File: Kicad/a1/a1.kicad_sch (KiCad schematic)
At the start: 123 parts, among them J1 Conn_02x03_Odd_Even, J2 VGA, J3 AudioJack4, J5 Conn_02x17_Odd_Even, J6 Barrel Jack, J7 DE9_Plug, J8 DE9_Plug, SW1 Q, SW10 P, SW11 A, SW12 S, SW13 D, SW14 F, SW15 G, SW16 H, SW17 J, SW18 K, SW19 L, SW2 W, SW20 ENTER, SW21 Z, SW22 X, SW23 C, SW24 V, SW25 SHIFT, SW26 ALT, SW27 B, SW28 N, SW29 M, SW3 E, SW30 SPACE, SW31 SW_Push, SW32 SW_SPDT, SW4 R, SW5 T, SW6 Y, SW7 U, SW8 I, SW9 O, U1 74HC590A, U10 74HC32, U11 74HC174, U12 74HC4520, U2 74HC590A, U3 62256, U4 SST39SF040, U5 W65C02SxP, U6 74HCT541, U7 74HC166, U8 74HC14, U9 74HC10, Y1 32Mhz

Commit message: Update pcb and readme
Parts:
- removed D37, D38, D5, D6: 1N4148, PCM_Diode_THT_AKL:D_DO-35_SOD27_P7.62mm_Horizontal, symbol PCM_Diode_AKL:1N4148
- removed J5: Conn_02x17_Odd_Even, Connector_IDC:IDC-Header_2x17_P2.54mm_Horizontal, symbol Connector_Generic:Conn_02x17_Odd_Even
- removed RN1: R_Network08, Resistor_THT:R_Array_SIP9, symbol Device:R_Network08
- added J4: Conn_02x17_Odd_Even, Connector_IDC:IDC-Header_2x17_P2.54mm_Horizontal, symbol Connector_Generic:Conn_02x17_Odd_Even
- added RN1: R_Network06, Resistor_THT:R_Array_SIP7, symbol Device:R_Network06
- BZ1: footprint Buzzer_Beeper:MagneticBuzzer_Kingstate_KCG0601 -> Connector_PinHeader_2.54mm:PinHeader_1x02_P2.54mm_Vertical
- D1: footprint LED_THT:LED_D3.0mm -> LED_THT:LED_Rectangular_W5.0mm_H2.0mm
- D10, D11, D12, D13, D14, D15, D16, D17, D18, D19, D20, D21, D22, D23, D24, D25, D26, D27, D28, D29, D30, D31, D32, D33, D34, D35, D36, D7, D8, D9: footprint PCM_Diode_THT_AKL:D_DO-35_SOD27_P7.62mm_Horizontal -> PCM_Diode_THT_AKL_Double:D_DO-35_SOD27_P7.62mm_Horizontal
- D2, D3, D4: footprint PCM_Diode_THT_AKL:D_DO-35_SOD27_P7.62mm_Horizontal -> Diode_THT:D_DO-34_SOD68_P2.54mm_Vertical_KathodeUp
- J3: footprint Connector_Audio:Jack_3.5mm_PJ320E_Horizontal -> Smal:Jack_3.5mm_PJ320A_Horizontal
- R1: value 1MΩ -> 1M; footprint PCM_Resistor_THT_AKL:R_Axial_DIN0204_L3.6mm_D1.6mm_P5.08mm_Horizontal -> PCM_Resistor_THT_AKL_Double:R_Axial_DIN0204_L3.6mm_D1.6mm_P5.08mm_Horizontal
- R11: value 5.6KΩ -> 5.6K; footprint PCM_Resistor_THT_US_AKL:R_Axial_DIN0204_L3.6mm_D1.6mm_P1.90mm_Vertical -> PCM_Resistor_THT_US_AKL:R_Axial_DIN0204_L3.6mm_D1.6mm_P2.54mm_Vertical
- R12, R13: value 27KΩ -> 27K; footprint PCM_Resistor_THT_US_AKL:R_Axial_DIN0204_L3.6mm_D1.6mm_P1.90mm_Vertical -> PCM_Resistor_THT_US_AKL:R_Axial_DIN0204_L3.6mm_D1.6mm_P2.54mm_Vertical
- R14: value 20KΩ -> 20K; footprint PCM_Resistor_THT_US_AKL:R_Axial_DIN0204_L3.6mm_D1.6mm_P1.90mm_Vertical -> PCM_Resistor_THT_US_AKL:R_Axial_DIN0204_L3.6mm_D1.6mm_P2.54mm_Vertical
- R2: value 180Ω -> 180; footprint PCM_Resistor_THT_AKL:R_Axial_DIN0204_L3.6mm_D1.6mm_P5.08mm_Horizontal -> PCM_Resistor_THT_AKL_Double:R_Axial_DIN0204_L3.6mm_D1.6mm_P5.08mm_Horizontal
- R3: value 150Ω -> 150; footprint PCM_Resistor_THT_AKL:R_Axial_DIN0204_L3.6mm_D1.6mm_P5.08mm_Horizontal -> PCM_Resistor_THT_AKL_Double:R_Axial_DIN0204_L3.6mm_D1.6mm_P5.08mm_Horizontal
- R4: value 330Ω -> 330; footprint PCM_Resistor_THT_AKL:R_Axial_DIN0204_L3.6mm_D1.6mm_P5.08mm_Horizontal -> PCM_Resistor_THT_US_AKL:R_Axial_DIN0204_L3.6mm_D1.6mm_P2.54mm_Vertical
- R5: value 100Ω -> 100; footprint PCM_Resistor_THT_US_AKL:R_Axial_DIN0204_L3.6mm_D1.6mm_P1.90mm_Vertical -> PCM_Resistor_THT_US_AKL:R_Axial_DIN0204_L3.6mm_D1.6mm_P2.54mm_Vertical
- SW20: value ENTER -> ENT
- U4: value SST39SF040 -> SST39SF0x0
- Y1: value 32Mhz -> 16Mhz
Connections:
- net COL 3 is gone; now on net A3: SW17.1, SW18.1, SW27.1, SW28.1, SW7.1, SW8.1
- net COL 4 is gone; now on net A4: SW10.1, SW19.1, SW20.1, SW29.1, SW30.1, SW9.1
- net A0: now also SW1.1, SW11.1, SW12.1, SW2.1, SW21.1, SW22.1, J4.11 (Pin_11); no longer D2.1 (K)
- net A1: now also SW13.1, SW14.1, SW23.1, SW24.1, SW3.1, SW4.1, J4.13 (Pin_13); no longer D3.1 (K)
- net A10: now also J4.31 (Pin_31)
- net A11: now also J8.8, J4.33 (Pin_33)
- net A12: now also J7.8, J4.34 (Pin_34)
- net A13: now also D3.2 (A), J4.32 (Pin_32)
- net A14: now also D2.2 (A), J4.30 (Pin_30)
- net A15: now also D4.2 (A), J4.28 (Pin_28)
- net A2: now also SW15.1, SW16.1, SW25.1, SW26.1, SW5.1, SW6.1, J4.15 (Pin_15); no longer D4.1 (K)
- net A3: now also J4.17 (Pin_17)
- net A4: now also J4.19 (Pin_19)
- net A5: now also J4.21 (Pin_21)
- net A6: now also J4.23 (Pin_23)
- net A7: now also J4.25 (Pin_25)
- net A8: now also J4.27 (Pin_27)
- net A9: now also J4.29 (Pin_29)
- net D0: now also J4.12 (Pin_12)
- net D1: now also J4.14 (Pin_14)
- net D2: now also J4.16 (Pin_16)
- net D3: now also J4.18 (Pin_18)
- net D4: now also J4.20 (Pin_20)
- net D5: now also J4.22 (Pin_22)
- net D6: now also J4.24 (Pin_24)
- net D7: now also J4.26 (Pin_26)
- net GND: now also J7.5, J8.5, R13.1, U12.1 (CK), J4.1 (Pin_1); no longer J2.15, R13.2, U11.1 (~{Mr})
- net HROW 0: now also RN1.7 (R6)
- net HROW 1: now also RN1.5 (R4)
- net HROW 2: now also RN1.4 (R3)
- net HROW 3: now also RN1.3 (R2)
- net HROW 4: now also RN1.6 (R5)
- net HROW 5: now also RN1.2 (R1)
- net M16: now also R1.2, R2.2, U12.2 (Enable), U8.8, J4.3 (Pin_3); no longer U12.3 (Q1)
- net M2: now also U12.5 (Q3); no longer U12.6 (Q4)
- net M4: now also U12.4 (Q2); no longer U12.5 (Q3)
- net M8: now also U12.3 (Q1); no longer U12.4 (Q2)
- net RAMHIDE: now also J4.7 (Pin_7)
- net V512: now also D2.1 (K), D3.1 (K), D4.1 (K)
- net VCC: now also J7.7, J8.7, U11.1 (~{Mr}), J4.2 (Pin_2), RN1.1 (common); no longer U12.2 (Enable)
- net r/~{w}: now also J4.10 (Pin_10)
- net ~{A13}: now also J4.9 (Pin_9)
- net ~{A15}: now also J4.8 (Pin_8)
- net ~{NMI}: now also J4.6 (Pin_6)
- net ~{RESET}: now also J4.5 (Pin_5)
- net ø2: now also J4.4 (Pin_4)
- net at R12.1, SW31.1: now also R13.2; no longer R13.1
- removed net COL 0: D2.2 (A), SW1.1, SW11.1, SW12.1, SW2.1, SW21.1, SW22.1
- removed net COL 1: D3.2 (A), SW13.1, SW14.1, SW23.1, SW24.1, SW3.1, SW4.1
- removed net COL 2: D4.2 (A), SW15.1, SW16.1, SW25.1, SW26.1, SW5.1, SW6.1
- no-connect marks 19 -> 17
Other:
- moved on the sheet: J1, R13, RN3

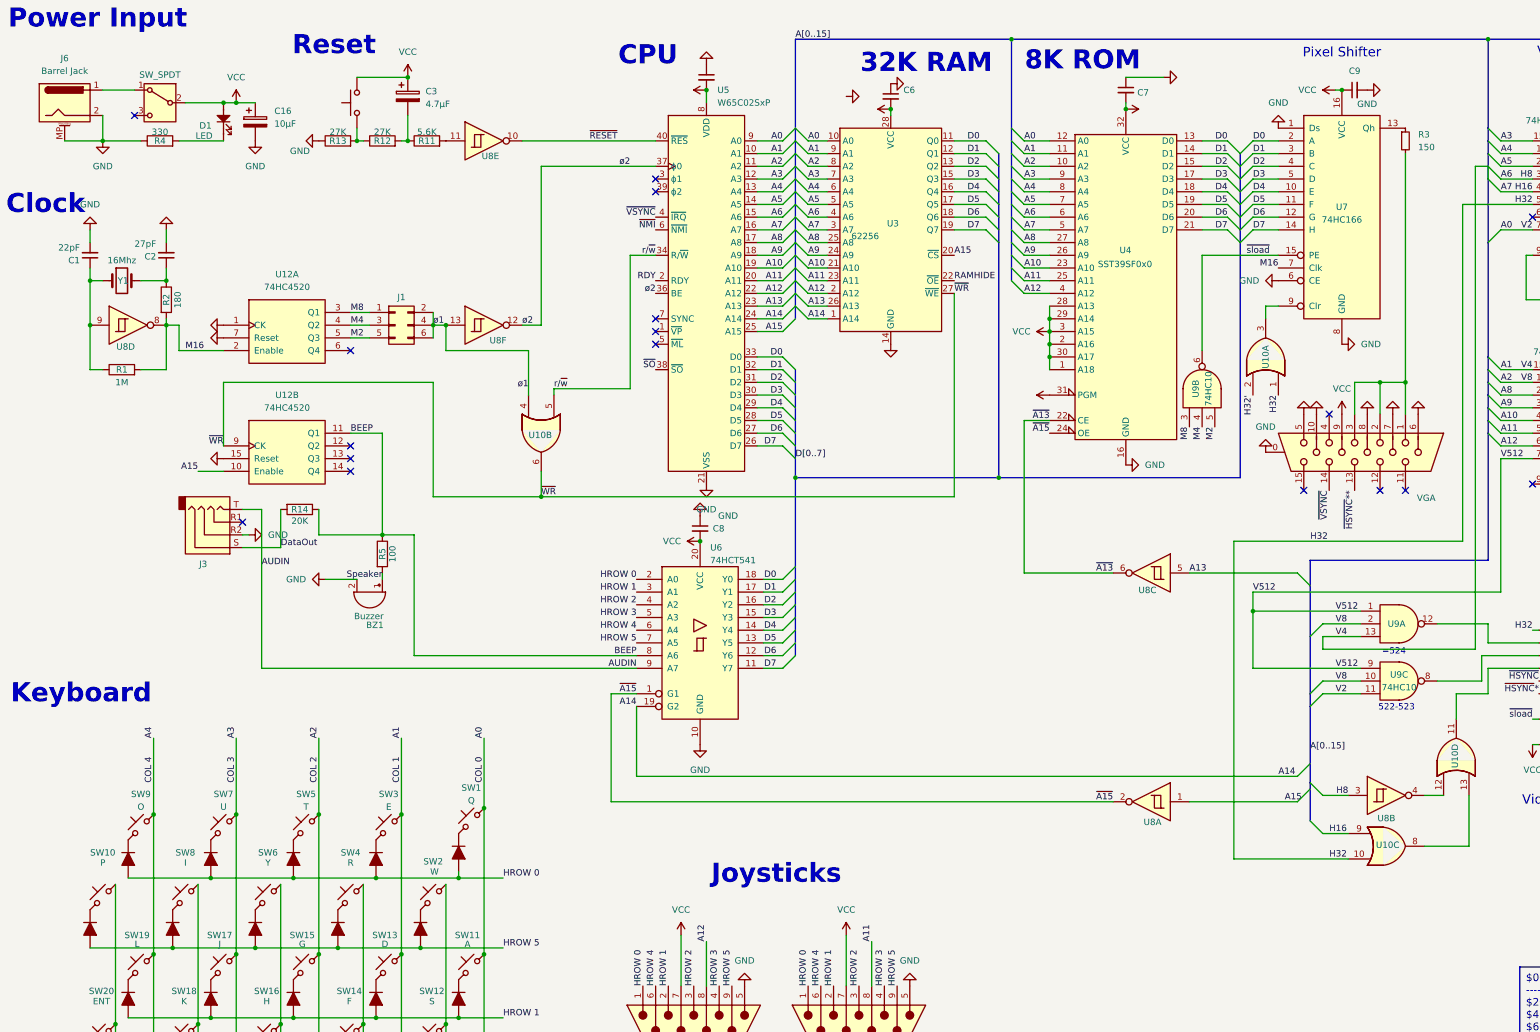
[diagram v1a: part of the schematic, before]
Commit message: tweak pcb, change key layout
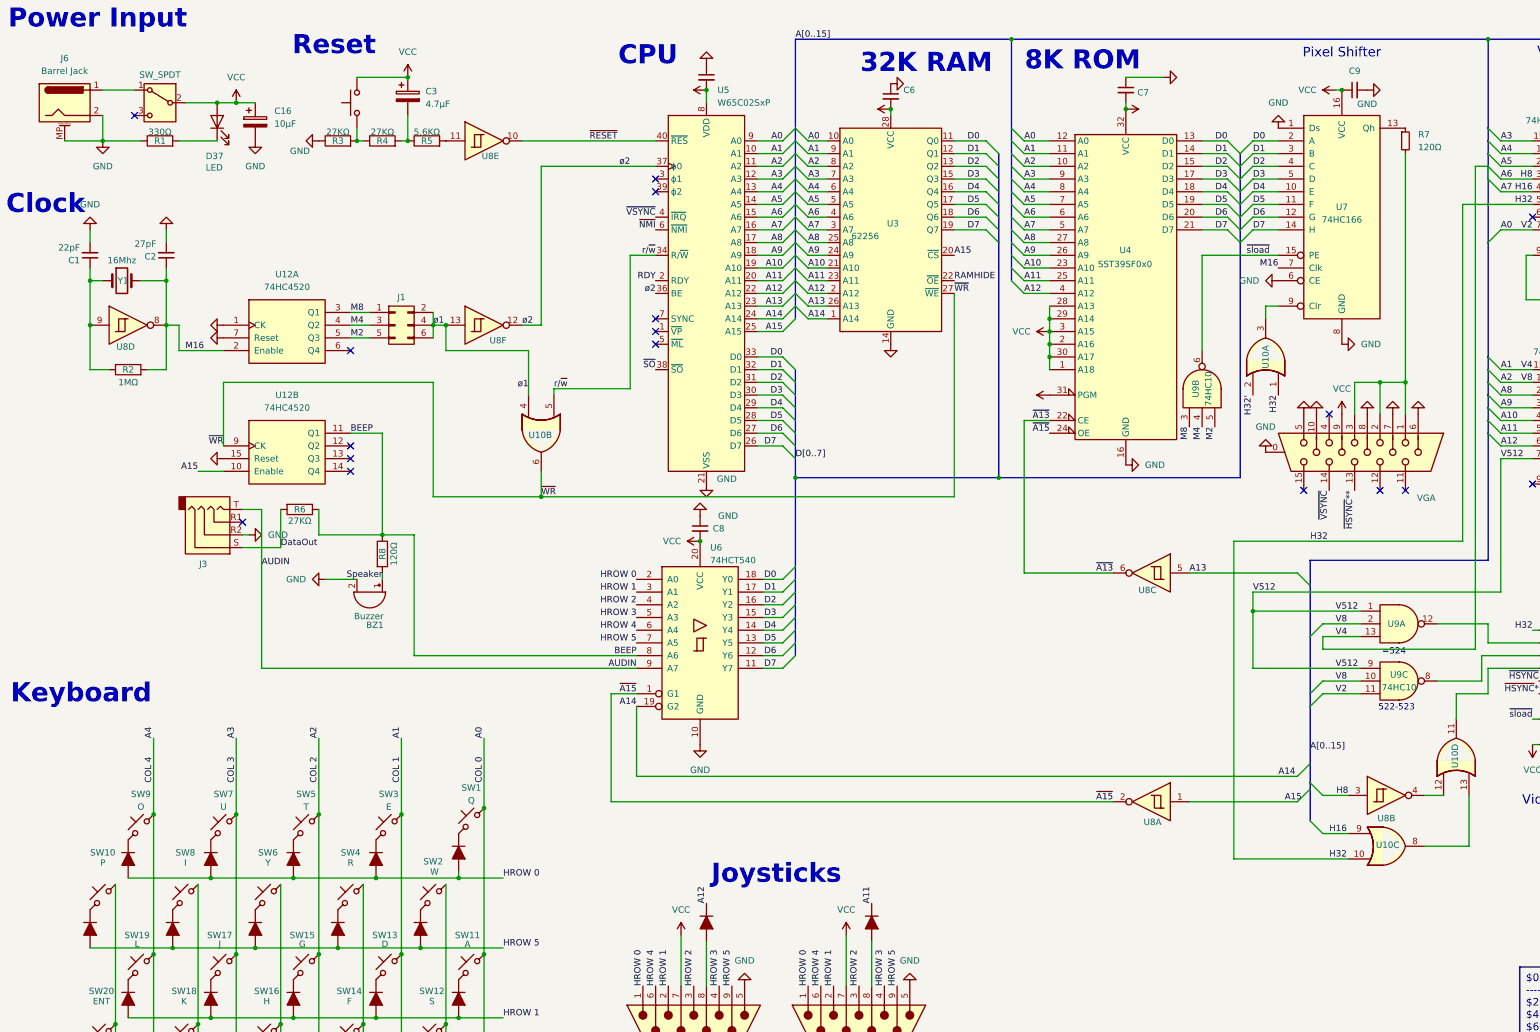
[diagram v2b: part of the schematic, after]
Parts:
- removed D1: LED, LED_THT:LED_Rectangular_W5.0mm_H2.0mm, symbol PCM_SL_Devices:LED
- removed R2: 180, PCM_Resistor_THT_AKL_Double:R_Axial_DIN0204_L3.6mm_D1.6mm_P5.08mm_Horizontal, symbol Device:R
- removed R5: 100, PCM_Resistor_THT_US_AKL:R_Axial_DIN0204_L3.6mm_D1.6mm_P2.54mm_Vertical, symbol Device:R
- added D37: LED, PCM_LED_THT_AKL:LED_Indicator_D3.0mm_W4.6mm_L6.5mm, symbol Device:LED
- added D5, D6: 1N4148, PCM_Diode_THT_AKL_Double:D_DO-35_SOD27_P7.62mm_Horizontal, symbol PCM_Diode_AKL:1N4148
- added R8: 120Ω, PCM_Resistor_THT_AKL_Double:R_Axial_DIN0204_L3.6mm_D1.6mm_P7.62mm_Horizontal, symbol Device:R
- BZ1: footprint Connector_PinHeader_2.54mm:PinHeader_1x02_P2.54mm_Vertical -> Buzzer_Beeper:MagneticBuzzer_Kingstate_KCG0601
- C3: footprint PCM_Capacitor_THT_AKL:CP_Radial_D5.0mm_P2.00mm -> PCM_Capacitor_THT_AKL:CP_Radial_D4.0mm_P1.50mm
- R1: renamed from R4; value 330 -> 330Ω; footprint PCM_Resistor_THT_US_AKL:R_Axial_DIN0204_L3.6mm_D1.6mm_P2.54mm_Vertical -> PCM_Resistor_THT_AKL_Double:R_Axial_DIN0204_L3.6mm_D1.6mm_P7.62mm_Horizontal
- R2: renamed from R1; value 1M -> 1MΩ; footprint PCM_Resistor_THT_AKL_Double:R_Axial_DIN0204_L3.6mm_D1.6mm_P5.08mm_Horizontal -> PCM_Resistor_THT_AKL_Double:R_Axial_DIN0204_L3.6mm_D1.6mm_P7.62mm_Horizontal
- R3: renamed from R13; value 27K -> 27KΩ; footprint PCM_Resistor_THT_US_AKL:R_Axial_DIN0204_L3.6mm_D1.6mm_P2.54mm_Vertical -> PCM_Resistor_THT_AKL_Double:R_Axial_DIN0204_L3.6mm_D1.6mm_P7.62mm_Horizontal
- R4: renamed from R12; value 27K -> 27KΩ; footprint PCM_Resistor_THT_US_AKL:R_Axial_DIN0204_L3.6mm_D1.6mm_P2.54mm_Vertical -> PCM_Resistor_THT_AKL_Double:R_Axial_DIN0204_L3.6mm_D1.6mm_P7.62mm_Horizontal
- R5: renamed from R11; value 5.6K -> 5.6KΩ; footprint PCM_Resistor_THT_US_AKL:R_Axial_DIN0204_L3.6mm_D1.6mm_P2.54mm_Vertical -> PCM_Resistor_THT_AKL_Double:R_Axial_DIN0204_L3.6mm_D1.6mm_P7.62mm_Horizontal
- R6: renamed from R14; value 20K -> 27KΩ; footprint PCM_Resistor_THT_US_AKL:R_Axial_DIN0204_L3.6mm_D1.6mm_P2.54mm_Vertical -> PCM_Resistor_THT_AKL_Double:R_Axial_DIN0204_L3.6mm_D1.6mm_P7.62mm_Horizontal
- R7: renamed from R3; value 150 -> 120Ω; footprint PCM_Resistor_THT_AKL_Double:R_Axial_DIN0204_L3.6mm_D1.6mm_P5.08mm_Horizontal -> PCM_Resistor_THT_AKL_Double:R_Axial_DIN0204_L3.6mm_D1.6mm_P7.62mm_Horizontal
- U6: value 74HCT541 -> 74HCT540
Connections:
- net A11: now also D5.1 (K); no longer J8.8
- net A12: now also D6.1 (K); no longer J7.8
- net BEEP: now also R8.1
- net M16: now also C2.1, Y1.2
- net Speaker: now also R8.2
- net VCC: now also D37.2 (A)
- net at R1.2: now also D37.1 (K)
- new net: D5.2 (A), J8.8
- new net: D6.2 (A), J7.8
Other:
- moved on the sheet: R2

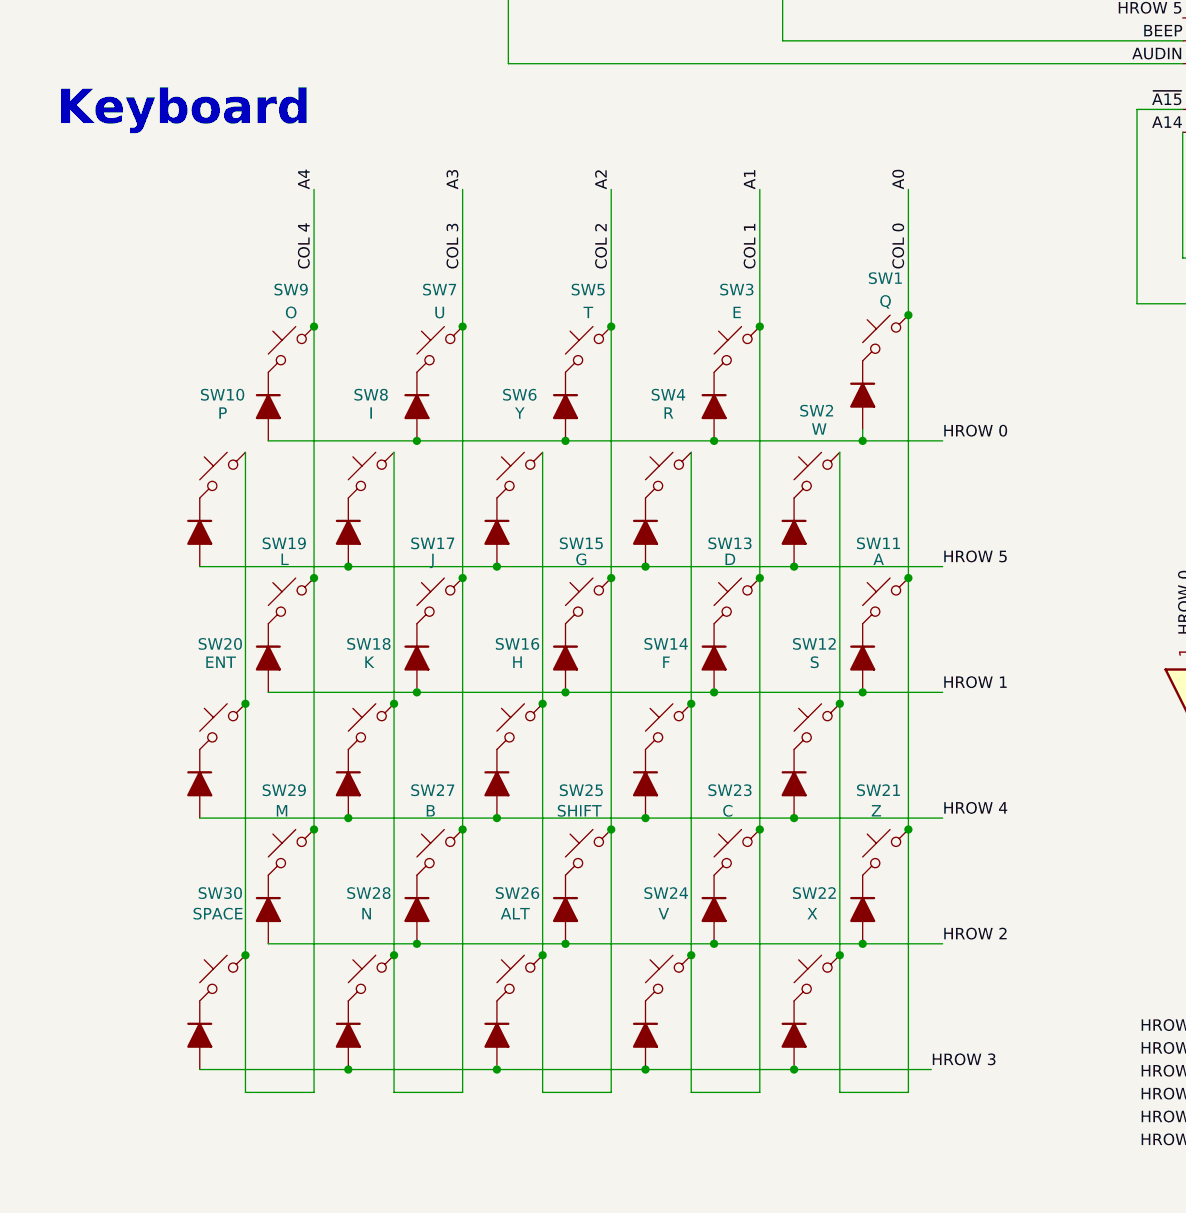
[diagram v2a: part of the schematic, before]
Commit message: Silkscreen tweaks
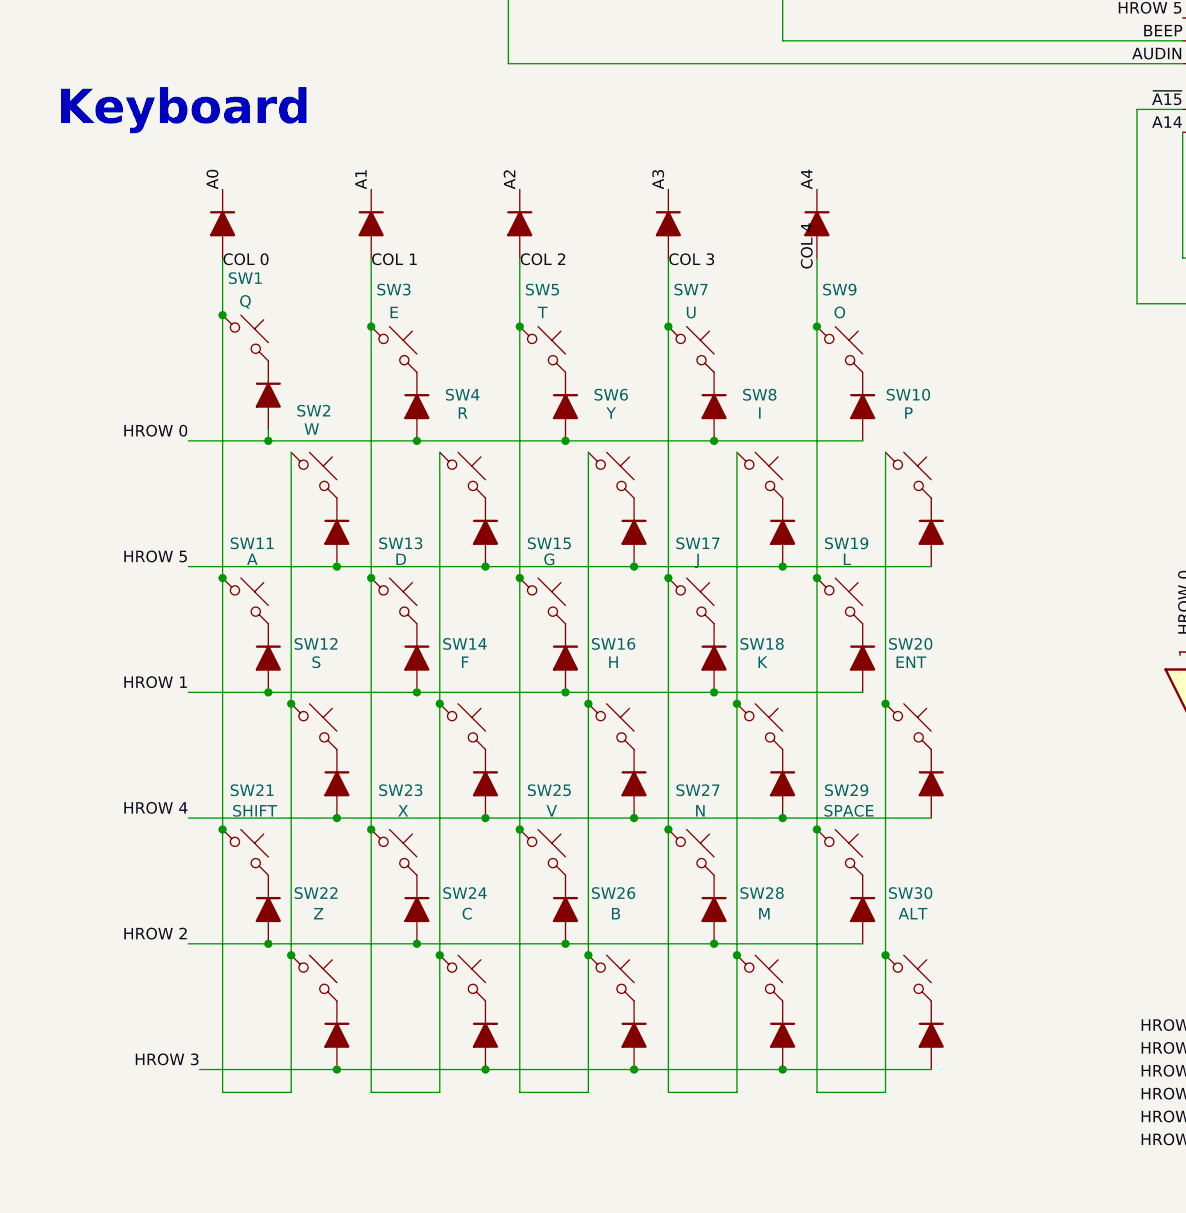
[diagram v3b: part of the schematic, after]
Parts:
- added D1, D38, D39, D40, D41: 1N4148, PCM_Diode_THT_AKL_Double:D_DO-35_SOD27_P7.62mm_Horizontal, symbol PCM_Diode_AKL:1N4148
- SW21: value Z -> SHIFT
- SW22: value X -> Z
- SW23: value C -> X
- SW24: value V -> C
- SW25: value SHIFT -> V
- SW26: value ALT -> B
- SW27: value B -> N
- SW28: value N -> M
- SW29: value M -> SPACE
- SW30: value SPACE -> ALT
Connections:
- net A0: now also D1.1 (K); no longer SW1.1, SW11.1, SW12.1, SW2.1, SW21.1, SW22.1
- net A1: now also D38.1 (K); no longer SW13.1, SW14.1, SW23.1, SW24.1, SW3.1, SW4.1
- net A2: now also D39.1 (K); no longer SW15.1, SW16.1, SW25.1, SW26.1, SW5.1, SW6.1
- net A3: now also D40.1 (K); no longer SW17.1, SW18.1, SW27.1, SW28.1, SW7.1, SW8.1
- net A4: now also D41.1 (K); no longer SW10.1, SW19.1, SW20.1, SW29.1, SW30.1, SW9.1
- new net COL 0: D1.2 (A), SW1.1, SW11.1, SW12.1, SW2.1, SW21.1, SW22.1
- new net COL 1: D38.2 (A), SW13.1, SW14.1, SW23.1, SW24.1, SW3.1, SW4.1
- new net COL 2: D39.2 (A), SW15.1, SW16.1, SW25.1, SW26.1, SW5.1, SW6.1
- new net COL 3: D40.2 (A), SW17.1, SW18.1, SW27.1, SW28.1, SW7.1, SW8.1
- new net COL 4: D41.2 (A), SW10.1, SW19.1, SW20.1, SW29.1, SW30.1, SW9.1
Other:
- moved on the sheet: SW1, SW10, SW11, SW12, SW13, SW14, SW15, SW16, SW17, SW18, SW19, SW2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

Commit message: Updated PCBs and Code
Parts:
- added C17: 100nF, PCM_Capacitor_THT_AKL_Double:C_Disc_D3.0mm_W1.6mm_P2.50mm, symbol Device:C_Small
- C1, C2: footprint Capacitor_THT:C_Disc_D3.0mm_W1.6mm_P2.50mm -> PCM_Capacitor_THT_AKL_Double:C_Disc_D3.0mm_W1.6mm_P2.50mm
- C10, C11, C12, C13, C14, C15, C4, C5, C6, C7, C8, C9: value C_Small -> 100nF; footprint Capacitor_THT:C_Disc_D3.0mm_W1.6mm_P2.50mm -> PCM_Capacitor_THT_AKL_Double:C_Disc_D3.0mm_W1.6mm_P2.50mm
- renumbered D41 to D37, D37 to D41
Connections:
- net DataOut: now also C17.1
- net GND: now also C17.2
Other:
- title: (none) -> MicroMicro
- moved on the sheet: C3, R3, R4, R5, U8E, Y1
